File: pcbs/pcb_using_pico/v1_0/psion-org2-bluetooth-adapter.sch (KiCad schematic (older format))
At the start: 18 parts, among them J1 Conn_02x08_Odd_Even, J5 Conn_01x04_Female, J7 Conn_01x03_Female, U1 74LS245, U2 74LS245, U3 Pico

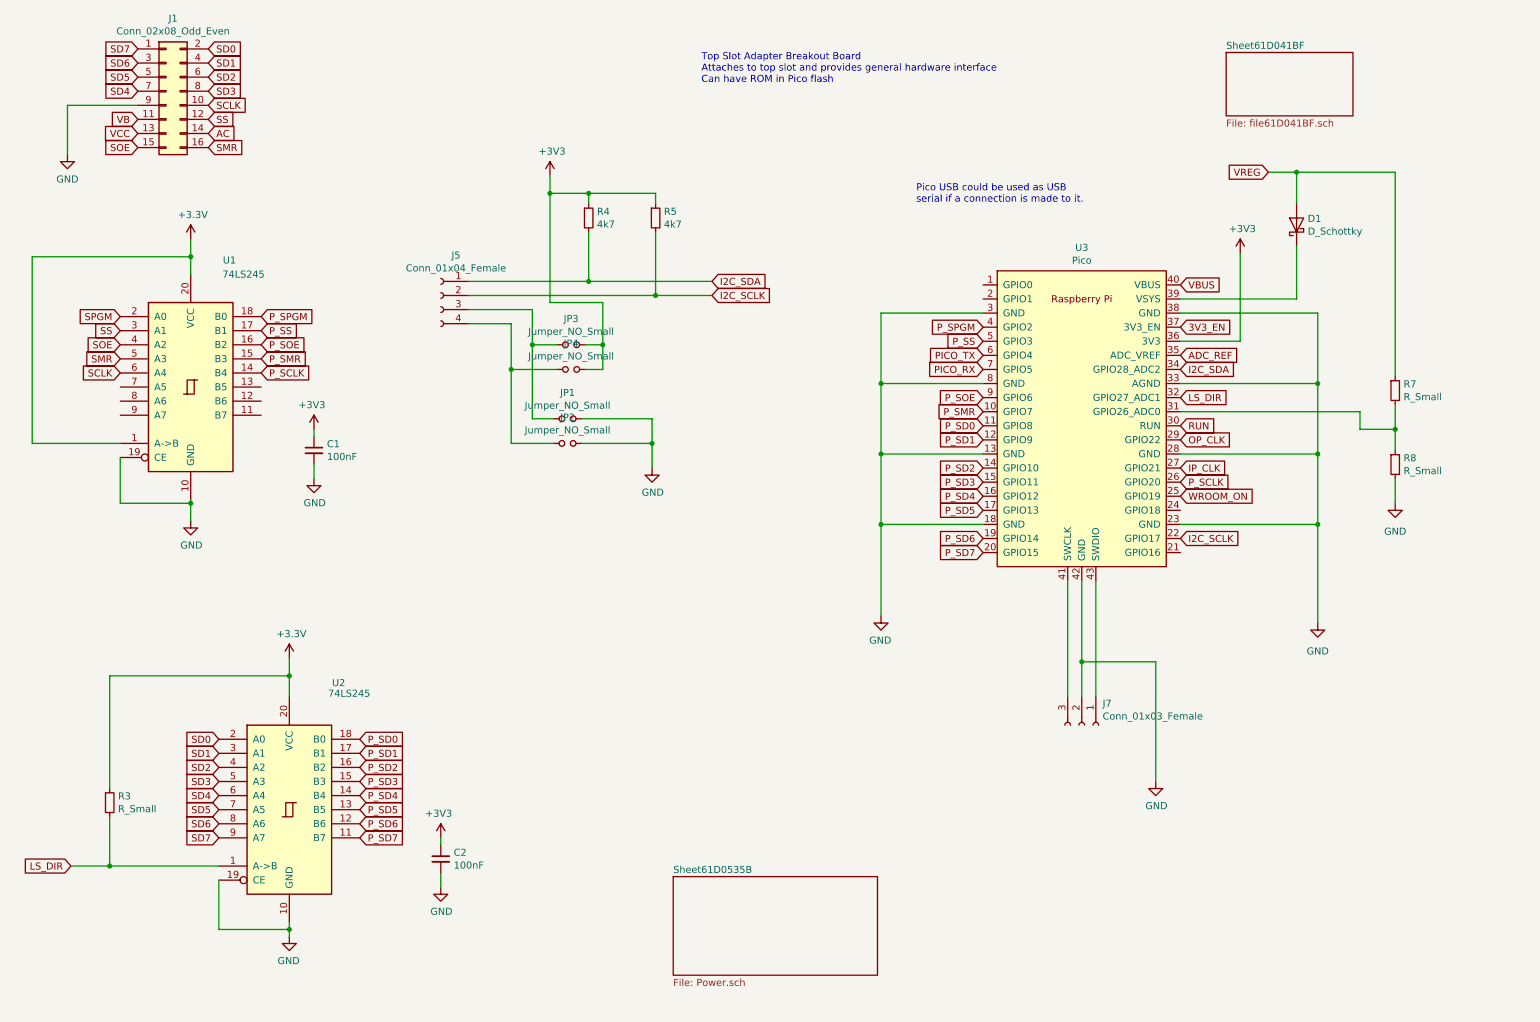
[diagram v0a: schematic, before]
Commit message: V2.0 sent off for fab. New charger IC with more solderable footprint, plus other fixes
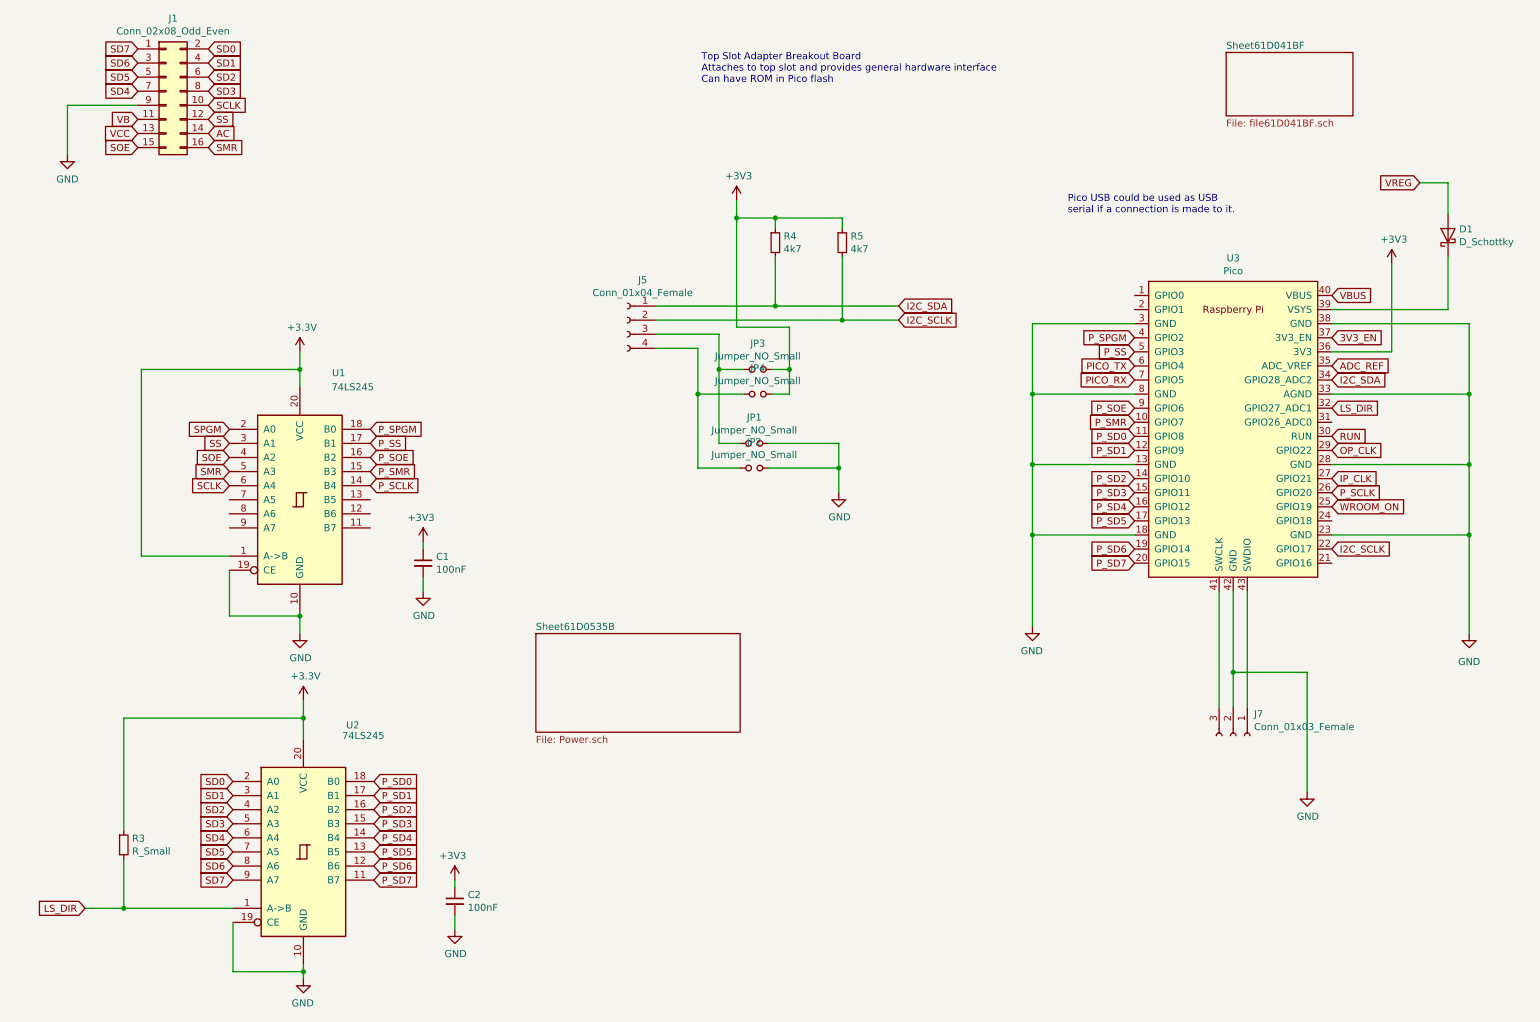
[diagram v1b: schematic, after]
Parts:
- removed R7, R8: R_Small, Resistor_SMD:R_0805_2012Metric, symbol Device:R_Small
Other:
- moved on the sheet: C1, C2, D1, J5, J7, JP1, JP2, JP3, JP4, R3, R4, R5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
